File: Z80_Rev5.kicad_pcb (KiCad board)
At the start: 2 copper layers, 88.5 x 64 mm, 25 parts, among them J2 UART, J3 I2C, J5 MicroSD, J7 USB_B_Mini, SW1 ON|OFF, SW2 Z80_RESET, SW3 CUSTOM, U1 Z84C00/PLCC, U3 AS6C4008-55PCN, U4 STC8H8K64U-45I-PDIP40, U5 SST39SF040

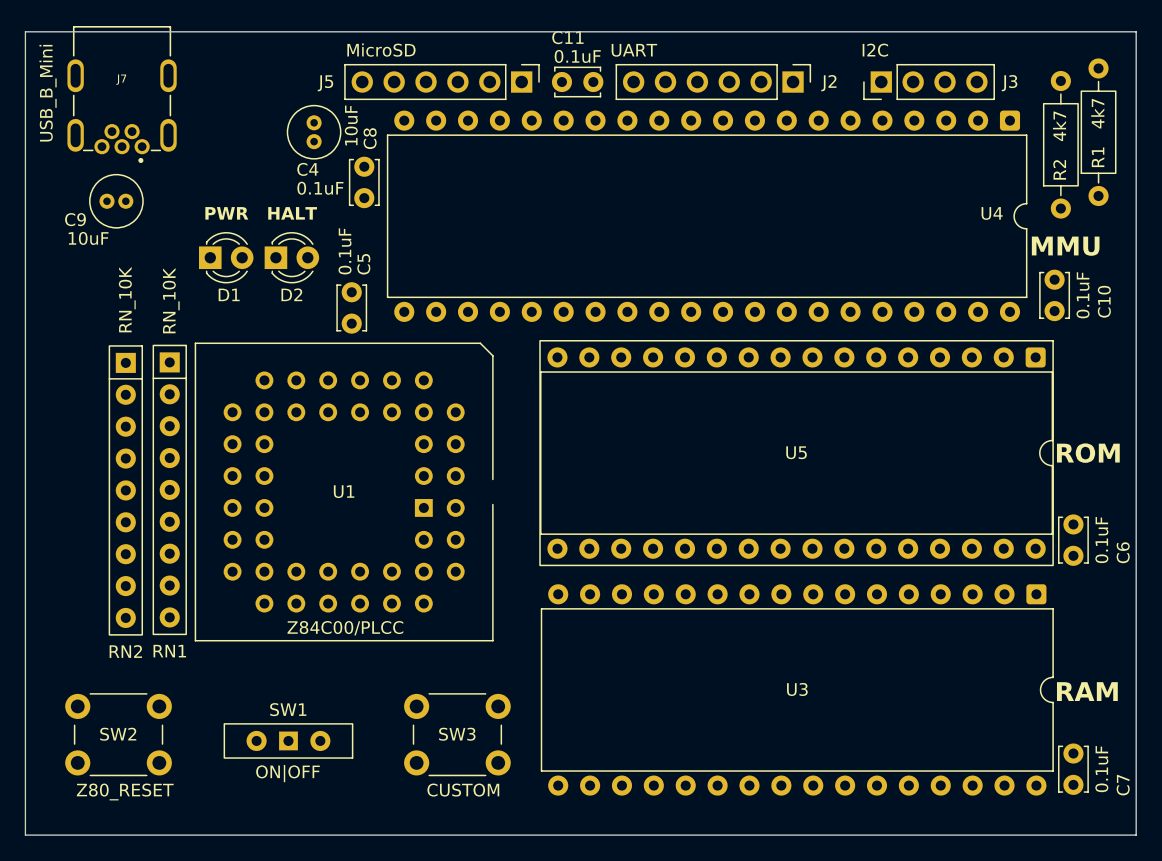
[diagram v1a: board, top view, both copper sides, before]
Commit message: Remove C4 because too many of them.
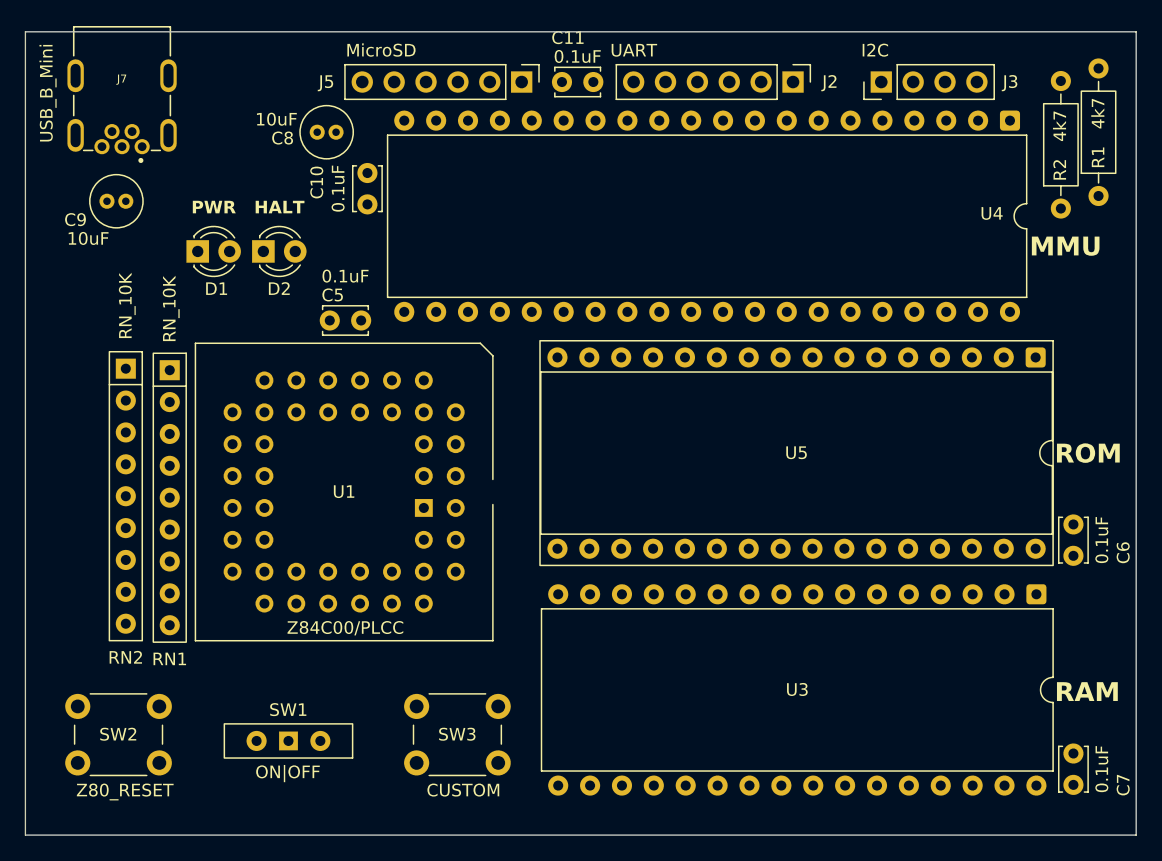
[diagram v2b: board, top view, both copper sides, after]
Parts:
- removed C4: 0.1uF, Capacitor_THT:C_Disc_D3.4mm_W2.1mm_P2.50mm
- moved C10 55.8 mm to (125.2, 60.8), turned to -90 degrees
- moved C5 2.37 mm to (124.8, 72.5), turned to 180 degrees
- moved D1 1.12 mm to (111.7, 67.0)
- moved D2 1.12 mm to (117.0, 67.0)
- moved C8 0.79 mm to (121.2, 57.5), turned to 0 degrees
- moved RN1 0.62 mm to (109.5, 76.5)
- moved RN2 0.46 mm to (106.0, 76.3)
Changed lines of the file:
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@@
 	(footprint "Resistor_THT:R_Array_SIP9"
 		(layer "F.Cu")
-		(at 106 75.88 -90)
+		(at 106 76.34 -90)
 		(descr "9-pin Resistor SIP pack")
 		(tags "R")
@@
 	(footprint "Capacitor_THT:C_Disc_D3.4mm_W2.1mm_P2.50mm"
 		(layer "F.Cu")
-		(at 124 70.25 -90)
+		(at 124.75 72.5 180)
 		(descr "C, Disc series, Radial, pin pitch=2.50mm, diameter*width=3.4*2.1mm^2, Capacitor, http://www.vishay.com/docs/45233/krseries.pdf")
 		(tags "C Disc series Radial pin pitch 2.50mm diameter 3.4mm width 2.1mm Capacitor")
 		(property "Reference" "C5"
-			(at -2.25 -1 90)
+			(at 2.25 2 0)
 			(layer "F.SilkS")
 			(effects
@@
 		)
 		(property "Value" "0.1uF"
-			(at -3.25 0.5 90)
+			(at 1.25 3.5 0)
 			(layer "F.SilkS")
 			(effects
@@
 		)
 		(property "Datasheet" ""
-			(at 0 0 90)
+			(at 0 0 0)
 			(layer "F.Fab")
 			(hide yes)
@@
 		)
 		(property "Description" "Unpolarized capacitor"
-			(at 0 0 90)
+			(at 0 0 0)
 			(layer "F.Fab")
 			(hide yes)
@@
 		(duplicate_pad_numbers_are_jumpers no)
 		(fp_line
-			(start -0.57 1.17)
-			(end -0.57 0.87)
-			(stroke
-				(width 0.12)
-				(type solid)
-			)
-			(layer "F.SilkS")
-		)
-		(fp_line
 			(start 3.07 1.17)
 			(end -0.57 1.17)
@@
 		)
 		(fp_line
-			(start -0.57 -0.87)
-			(end -0.57 -1.17)
-			(stroke
-				(width 0.12)
-				(type solid)
-			)
-			(layer "F.SilkS")
-		)
-		(fp_line
-			(start -0.57 -1.17)
-			(end 3.07 -1.17)
-			(stroke
-				(width 0.12)
-				(type solid)
-			)
-			(layer "F.SilkS")
-		)
-		(fp_line
 			(start 3.07 -1.17)
 			(end 3.07 -0.87)
@@
 			(layer "F.SilkS")
 		)
-		(fp_rect
-			(start -1.05 -1.3)
-			(end 3.55 1.3)
-			(stroke
-				(width 0.05)
-				(type solid)
-			)
-			(fill no)
-			(layer "F.CrtYd")
-		)
-		(fp_rect
-			(start -0.45 -1.05)
-			(end 2.95 1.05)
-			(stroke
-				(width 0.1)
-				(type solid)
-			)
-			(fill no)
-			(layer "F.Fab")
-		)
-		(fp_text user "${REFERENCE}"
-			(at 1.25 0 90)
-			(layer "F.Fab")
-			(effects
-				(font
-					(size 0.68 0.68)
-					(thickness 0.102)
-				)
-			)
-		)
-		(pad "1" thru_hole circle
-			(at 0 0 270)
-			(size 1.6 1.6)
-			(drill 0.8)
-			(layers "*.Cu" "*.Mask")
-			(remove_unused_layers no)
-			(net "GND")
-			(pintype "passive")
-		)
-		(pad "2" thru_hole circle
-			(at 2.5 0 270)
-			(size 1.6 1.6)
-			(drill 0.8)
-			(layers "*.Cu" "*.Mask")
-			(remove_unused_layers no)
-			(net "VCC")
-			(pintype "passive")
-		)
-		(embedded_fonts no)
-		(model "${KICAD10_3DMODEL_DIR}/Capacitor_THT.3dshapes/C_Disc_D3.4mm_W2.1mm_P2.50mm.step"
-			(offset
-				(xyz 0 0 0)
-			)
-			(scale
-				(xyz 1 1 1)
-			)
-			(rotate
-				(xyz 0 0 0)
-			)
-		)
-	)
-	(footprint "Capacitor_THT:C_Disc_D3.4mm_W2.1mm_P2.50mm"
-		(layer "F.Cu")
-		(at 125 60.25 -90)
-		(descr "C, Disc series, Radial, pin pitch=2.50mm, diameter*width=3.4*2.1mm^2, Capacitor, http://www.vishay.com/docs/45233/krseries.pdf")
-		(tags "C Disc series Radial pin pitch 2.50mm diameter 3.4mm width 2.1mm Capacitor")
-		(property "Reference" "C4"
-			(at 0.25 4.5 180)
-			(layer "F.SilkS")
-			(effects
-				(font
-					(size 1 1)
-					(thickness 0.15)
-				)
-			)
-		)
-		(property "Value" "0.1uF"
-			(at 1.75 3.5 180)
-			(layer "F.SilkS")
-			(effects
-				(font
-					(size 1 1)
-					(thickness 0.15)
-				)
-			)
-		)
-		(property "Datasheet" ""
-			(at 0 0 90)
-			(layer "F.Fab")
-			(hide yes)
-			(effects
-				(font
-					(size 1.27 1.27)
-				)
-			)
-		)
-		(property "Description" "Unpolarized capacitor"
-			(at 0 0 90)
-			(layer "F.Fab")
-			(hide yes)
-			(effects
-				(font
-					(size 1.27 1.27)
-				)
-			)
-		)
-		(property ki_fp_filters "C_*")
-		(sheetname "/")
-		(sheetfile "Z80_Rev5.kicad_sch")
-		(units
-			(unit
-				(name "A")
-				(pins "1" "2")
-			)
-		)
-		(attr through_hole)
-		(duplicate_pad_numbers_are_jumpers no)
 		(fp_line
 			(start -0.57 1.17)
@@
 		)
 		(fp_line
-			(start 3.07 1.17)
-			(end -0.57 1.17)
-			(stroke
-				(width 0.12)
-				(type solid)
-			)
-			(layer "F.SilkS")
-		)
-		(fp_line
-			(start 3.07 0.87)
-			(end 3.07 1.17)
-			(stroke
-				(width 0.12)
-				(type solid)
-			)
-			(layer "F.SilkS")
-		)
-		(fp_line
 			(start -0.57 -0.87)
 			(end -0.57 -1.17)
@@
 			(layer "F.SilkS")
 		)
-		(fp_line
-			(start 3.07 -1.17)
-			(end 3.07 -0.87)
-			(stroke
-				(width 0.12)
-				(type solid)
-			)
-			(layer "F.SilkS")
-		)
 		(fp_rect
 			(start -1.05 -1.3)
@@
 		)
 		(fp_text user "${REFERENCE}"
-			(at 1.25 0 90)
+			(at 1.25 0 0)
 			(layer "F.Fab")
 			(effects
@@
 		)
 		(pad "1" thru_hole circle
-			(at 0 0 270)
+			(at 0 0 180)
 			(size 1.6 1.6)
 			(drill 0.8)
@@
 		)
 		(pad "2" thru_hole circle
-			(at 2.5 0 270)
+			(at 2.5 0 180)
 			(size 1.6 1.6)
 			(drill 0.8)
@@
 	(footprint "Capacitor_THT:C_Radial_D4.0mm_H5.0mm_P1.50mm"
 		(layer "F.Cu")
-		(at 121 58.25 90)
+		(at 121.25 57.5)
 		(descr "C, Radial series, Radial, pin pitch=1.50mm, diameter=4mm, height=5mm, Non-Polar Electrolytic Capacitor")
 		(tags "C Radial series Radial pin pitch 1.50mm diameter 4mm height 5mm Non-Polar Electrolytic Capacitor")
 		(property "Reference" "C8"
-			(at 0.25 4.5 90)
+			(at -2.75 0.5 0)
 			(layer "F.SilkS")
 			(effects
@@
 		)
 		(property "Value" "10uF"
-			(at 1.25 3 90)
+			(at -3.25 -1 0)
 			(layer "F.SilkS")
 			(effects
@@
 		)
 		(property "Datasheet" ""
-			(at 0 0 90)
+			(at 0 0 0)
 			(layer "F.Fab")
 			(hide yes)
@@
 		)
 		(property "Description" "Unpolarized capacitor"
-			(at 0 0 90)
+			(at 0 0 0)
 			(layer "F.Fab")
 			(hide yes)
@@
 		)
 		(fp_text user "${REFERENCE}"
-			(at 0.75 0 90)
+			(at 0.75 0 0)
 			(layer "F.Fab")
 			(effects
@@
 		)
 		(pad "1" thru_hole circle
-			(at 0 0 90)
+			(at 0 0)
 			(size 1.2 1.2)
 			(drill 0.6)
@@
 		)
 		(pad "2" thru_hole circle
-			(at 1.5 0 90)
+			(at 1.5 0)
 			(size 1.2 1.2)
 			(drill 0.6)
@@
 	(footprint "Resistor_THT:R_Array_SIP9"
 		(layer "F.Cu")
-		(at 109.5 75.84 -90)
+		(at 109.5 76.46 -90)
 		(descr "9-pin Resistor SIP pack")
 		(tags "R")
@@
 	(footprint "LED_THT:LED_D3.0mm"
 		(layer "F.Cu")
-		(at 112.73 67.5)
+		(at 111.73 67)
 		(descr "LED, diameter 3.0mm, 2 pins, generated by kicad-footprint-generator")
 		(tags "LED")
@@
 		)
 		(point
-			(at 114 67.5)
+			(at 113 67)
 			(size 2)
 			(layer "F.Fab")
@@
 	(footprint "LED_THT:LED_D3.0mm"
 		(layer "F.Cu")
-		(at 117.96 67.5)
+		(at 116.96 67)
 		(descr "LED, diameter 3.0mm, 2 pins, generated by kicad-footprint-generator")
 		(tags "LED")
@@
 		)
 		(point
-			(at 119.23 67.5)
+			(at 118.23 67)
 			(size 2)
 			(layer "F.Fab")
@@
 	(footprint "Capacitor_THT:C_Disc_D3.4mm_W2.1mm_P2.50mm"
 		(layer "F.Cu")
-		(at 180 71.75 90)
+		(at 125.25 60.75 -90)
 		(descr "C, Disc series, Radial, pin pitch=2.50mm, diameter*width=3.4*2.1mm^2, Capacitor, http://www.vishay.com/docs/45233/krseries.pdf")
 		(tags "C Disc series Radial pin pitch 2.50mm diameter 3.4mm width 2.1mm Capacitor")
@@
 		(duplicate_pad_numbers_are_jumpers no)
 		(fp_line
-			(start 3.07 -1.17)
-			(end 3.07 -0.87)
+			(start -0.57 1.17)
+			(end -0.57 0.87)
 			(stroke
 				(width 0.12)
@@
 		)
 		(fp_line
-			(start -0.57 -1.17)
-			(end 3.07 -1.17)
+			(start 3.07 1.17)
+			(end -0.57 1.17)
 			(stroke
 				(width 0.12)
@@
 		)
 		(fp_line
-			(start -0.57 -0.87)
-			(end -0.57 -1.17)
+			(start 3.07 0.87)
+			(end 3.07 1.17)
 			(stroke
 				(width 0.12)
@@
 		)
 		(fp_line
-			(start 3.07 0.87)
-			(end 3.07 1.17)
+			(start -0.57 -0.87)
+			(end -0.57 -1.17)
 			(stroke
 				(width 0.12)
@@
 		)
 		(fp_line
-			(start 3.07 1.17)
-			(end -0.57 1.17)
+			(start -0.57 -1.17)
+			(end 3.07 -1.17)
 			(stroke
 				(width 0.12)
@@
 		)
 		(fp_line
-			(start -0.57 1.17)
-			(end -0.57 0.87)
+			(start 3.07 -1.17)
+			(end 3.07 -0.87)
 			(stroke
 				(width 0.12)
@@
 		)
 		(pad "1" thru_hole circle
-			(at 0 0 90)
+			(at 0 0 270)
 			(size 1.6 1.6)
 			(drill 0.8)
@@
 		)
 		(pad "2" thru_hole circle
-			(at 2.5 0 90)
+			(at 2.5 0 270)
 			(size 1.6 1.6)
 			(drill 0.8)

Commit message: Routing...
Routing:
- net /MEM_A18: track 0.00 -> 133.9 mm, vias 0 -> 5
- net /MEM_A16: track 0.00 -> 114.7 mm, vias 0 -> 3
- net /BUTTON: track 0.00 -> 113.2 mm, vias 0 -> 5
- net /A0: track 0.00 -> 78.5 mm
- net Net-(J7-VBUS): track 0.00 -> 61.1 mm, vias 0 -> 1
- net /RAM_CE: track 0.00 -> 58.8 mm, vias 0 -> 4
- net /MEM_A15: track 0.00 -> 57.1 mm, vias 0 -> 1
- net /A1: track 0.00 -> 56.7 mm
- net /MEM_A17: track 0.00 -> 56.1 mm, vias 0 -> 3
- net /A3: track 0.00 -> 55.7 mm, vias 0 -> 2
- net /D7: track 0.00 -> 54.6 mm
- net /D6: track 0.00 -> 53.5 mm
- net /D5: track 0.00 -> 52.5 mm
- net /D3: track 0.00 -> 52.0 mm
- net /D4: track 0.00 -> 51.7 mm
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- added copper zone on B.Cu, net GND
- added copper zone on F.Cu, net VCC
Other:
- outline, holes or cut-outs redrawn
